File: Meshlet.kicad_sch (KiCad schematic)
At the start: 93 parts, among them J1 Ext. Notif. Header, J10 STEMMA QT I2C, J11 GPIO Exp., J12 I2C PINHEADER, J2 USB_C_Receptacle_USB2.0_16P, J3 Ext. Power Header, J4 Batt. Header (JST-PH 2.0), J5 SWD, J6 Batt. Header (Picoblade 1.25), J7 GPS Header, J8 User Btn Header, J9 Power Switch, Q1 AO3400A, SW1 BOOTSEL, SW3 RST, U1 W25Q32JVZP, U2 XC6206PxxxMR, U3 RP2350_60QFN, U4 INA3221, U5 BME280, U6 Wio-SX1262, U7 USBLC6-2SC6, U8 BQ24074RGT, Y1 12.000MHz

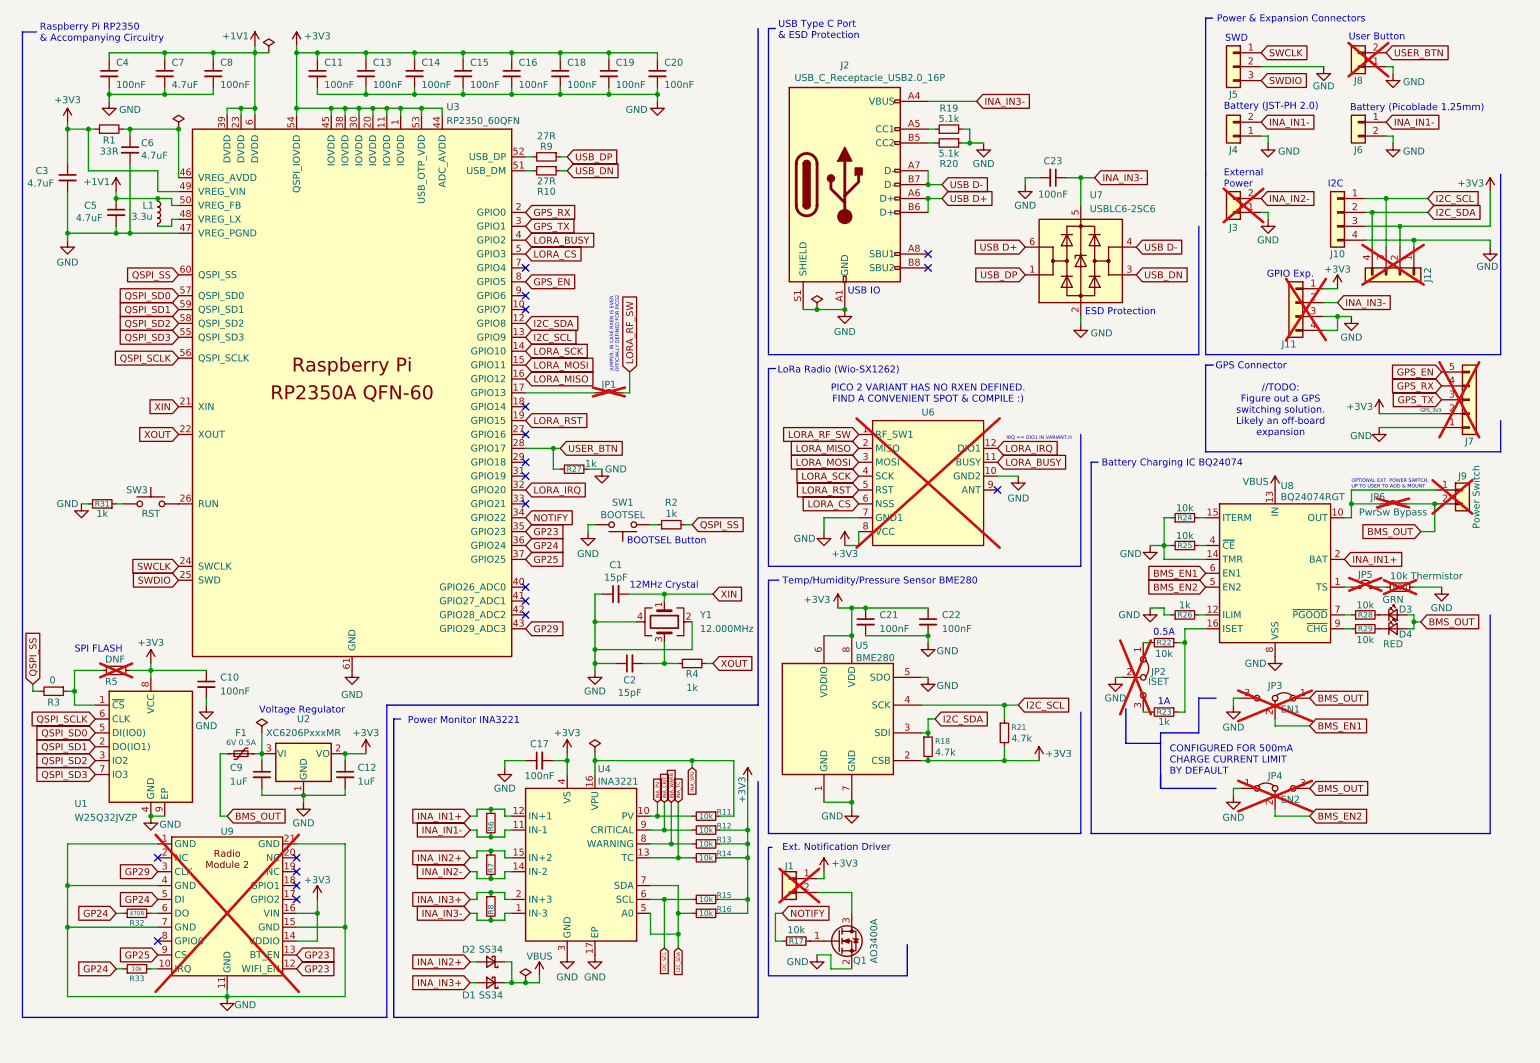
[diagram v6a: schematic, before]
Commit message: Silkscreen changes, added BQ24074 output breakout
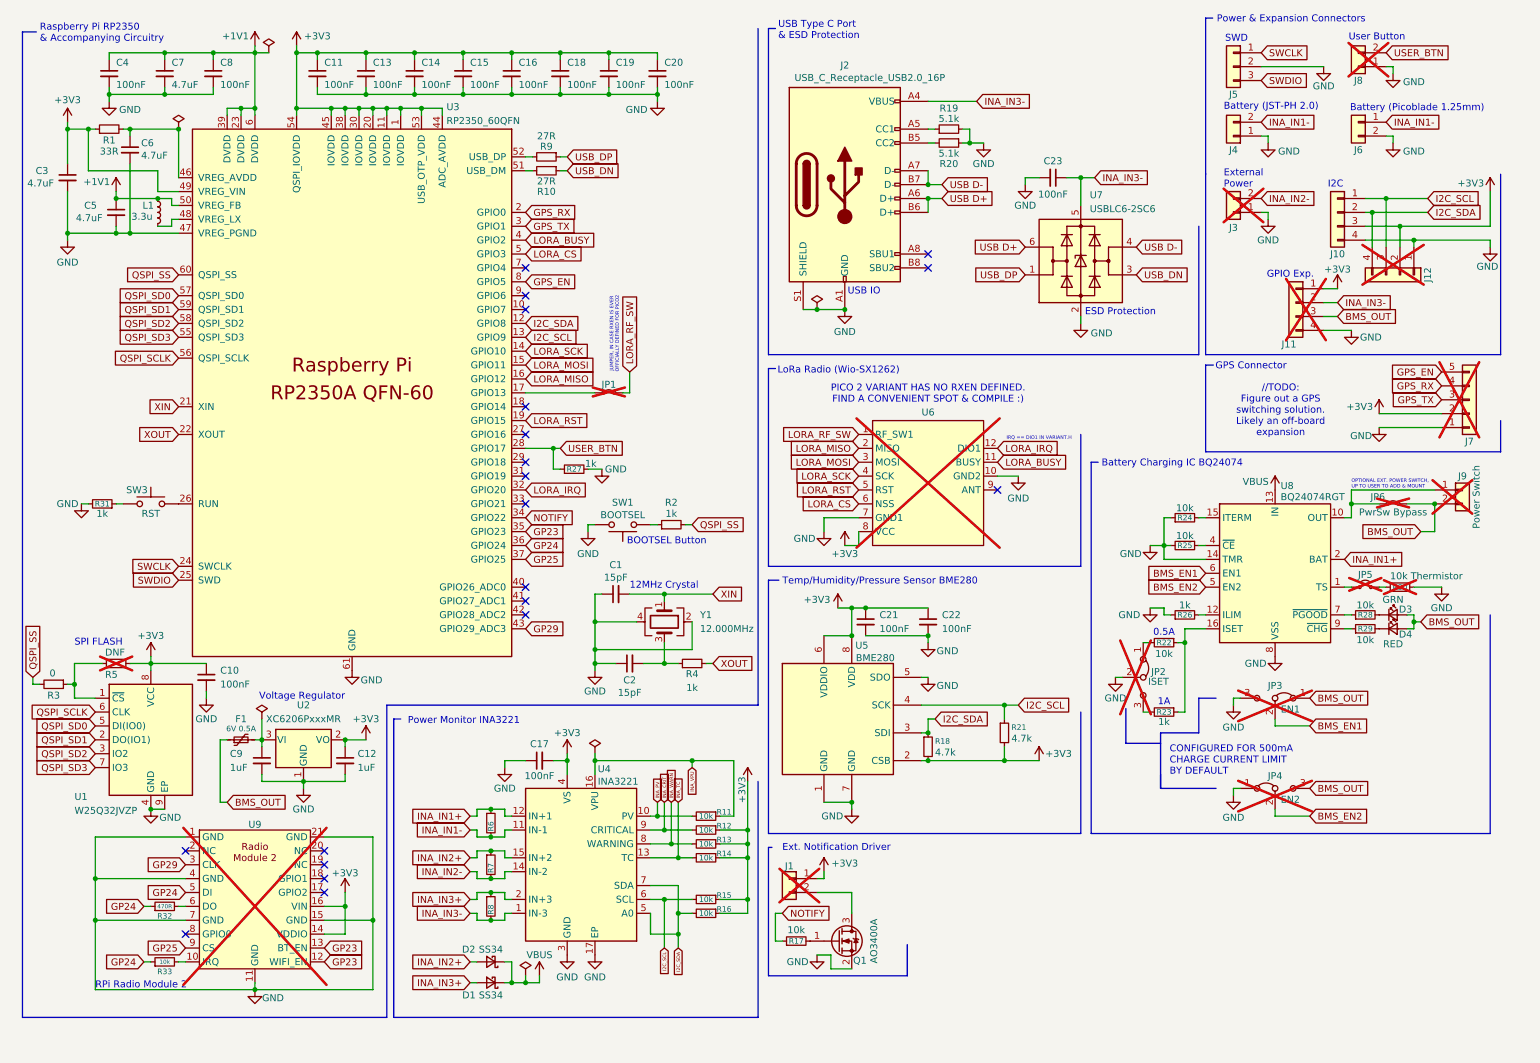
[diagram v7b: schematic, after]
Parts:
- R6, R7, R8: value PT2512FK-070R1L -> PA2512FKF7W0R01E
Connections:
- net BMS_OUT: now also J11.3 (Pin_3)
- net GND: no longer J11.3 (Pin_3)
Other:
- note added: "RPi Radio Module 2"
- moved on the sheet: C10, C12, C9, F1, R3, R32, R33, R5, U1, U2, U9

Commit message: Fixed several design flaws. More caps, more LDOs, etc
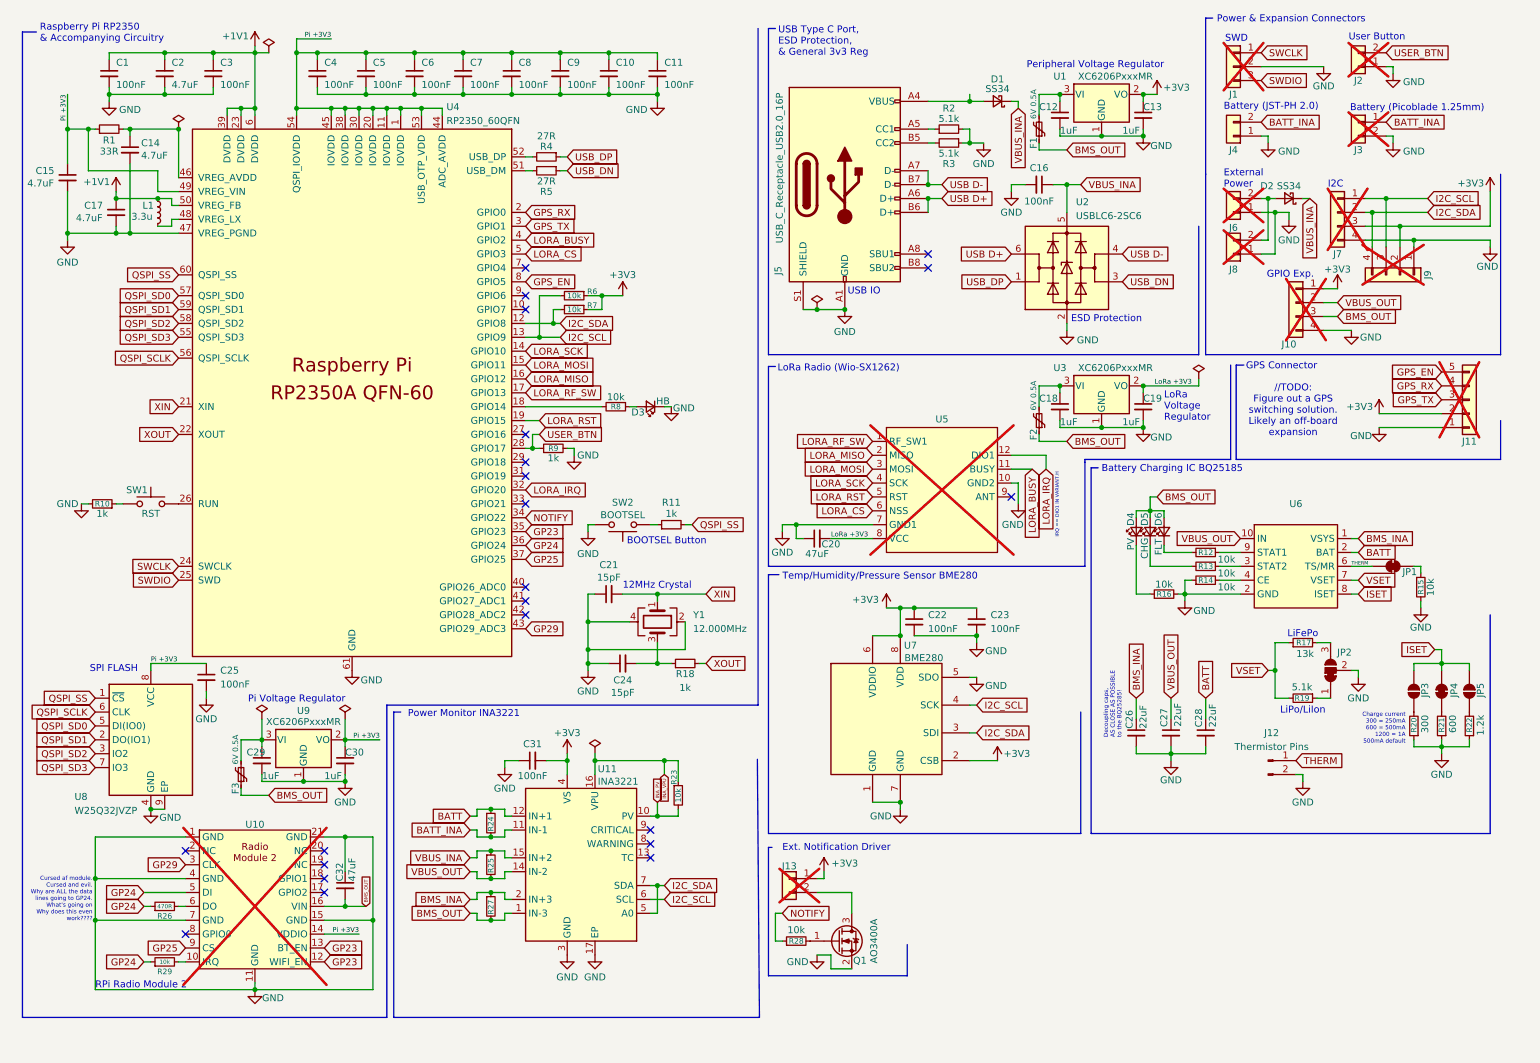
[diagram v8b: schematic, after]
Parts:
- removed J9: Power Switch, Connector_PinHeader_2.00mm:PinHeader_1x02_P2.00mm_Vertical, symbol Connector_Generic:Conn_01x02
- removed JP1: RF_SW Jumper, Jumper:SolderJumper-2_P1.3mm_Bridged_RoundedPad1.0x1.5mm, symbol Jumper:Jumper_2_Small_Bridged
- removed JP2: ISET, Jumper:SolderJumper-3_P1.3mm_Bridged12_RoundedPad1.0x1.5mm, symbol Jumper:Jumper_3_Bridged12
- removed JP3: EN1, Jumper:SolderJumper-3_P1.3mm_Bridged12_RoundedPad1.0x1.5mm, symbol Jumper:Jumper_3_Bridged12
- removed JP4: EN2, Jumper:SolderJumper-3_P1.3mm_Bridged12_RoundedPad1.0x1.5mm, symbol Jumper:Jumper_3_Bridged12
- removed JP5: BMS TS Jumper, Jumper:SolderJumper-2_P1.3mm_Open_RoundedPad1.0x1.5mm, symbol Jumper:Jumper_2_Small_Open
- removed JP6: PwrSw Bypass, Jumper:SolderJumper-2_P1.3mm_Bridged_RoundedPad1.0x1.5mm, symbol Jumper:Jumper_2_Small_Bridged
- removed R12, R13, R14, R24: 10k, Resistor_SMD:R_0402_1005Metric, symbol Device:R_Small
- removed R18: 4.7k, Resistor_SMD:R_0402_1005Metric, symbol Device:R_Small
- removed R23, R26: 1k, Resistor_SMD:R_0402_1005Metric, symbol Device:R_Small
- removed R3: 0, Resistor_SMD:R_0402_1005Metric, symbol Device:R_Small
- removed R30: 10k Thermistor, Resistor_SMD:R_0402_1005Metric, symbol Device:R_Small
- removed R5: DNF, Resistor_SMD:R_0402_1005Metric, symbol Device:R_Small
- removed U8: BQ24074RGT, Package_DFN_QFN:VQFN-16-1EP_3x3mm_P0.5mm_EP1.6x1.6mm, symbol Battery_Management:BQ24074RGT
- added C12, C13, C18, C19: 1uF, Capacitor_SMD:C_0402_1005Metric, symbol Device:C_Small
- added C20, C32: 47uF, Capacitor_SMD:C_0805_2012Metric, symbol Device:C_Small
- added C26, C27, C28: 22uF, symbol Device:C_Small
- added D3: HB, LED_SMD:LED_0603_1608Metric, symbol Device:LED_Small
- added D4: PV, LED_SMD:LED_0603_1608Metric, symbol Device:LED_Small
- added F1, F2: 6V 0.5A, Fuse:Fuse_0603_1608Metric, symbol Device:Polyfuse_Small
- added J12: Thermistor Pins, symbol Connector:Conn_01x02_Pin
- added J8: Ext. Power Header, Connector_PinHeader_2.54mm:PinHeader_1x02_P2.54mm_Vertical, symbol Connector_Generic:Conn_01x02
- added JP1: TS, symbol Jumper:SolderJumper_2_Bridged
- added JP2: Chemistry Select, symbol Jumper:SolderJumper_3_Bridged12
- added JP3, JP5: SolderJumper_2_Open, symbol Jumper:SolderJumper_2_Open
- added JP4: SolderJumper_2_Bridged, symbol Jumper:SolderJumper_2_Bridged
- added R15, R16, R8: 10k, Resistor_SMD:R_0402_1005Metric, symbol Device:R_Small
- added R17: 13k, symbol Device:R_Small
- added R19: 5.1k, symbol Device:R_Small
- added R20: 300, symbol Device:R_Small
- added U1, U3: XC6206PxxxMR, Package_TO_SOT_SMD:SOT-23-3, symbol Regulator_Linear:XC6206PxxxMR
- added U6: ~, symbol BQ25185:BQ25185
- D5: renamed from D3; value GRN -> CHG
- D6: renamed from D4; value RED -> FLT
- J1: renamed from J5; now not fitted
- J3: renamed from J6; now not fitted
- J7: renamed from J10; now not fitted
- R21: value 4.7k -> 600; footprint Resistor_SMD:R_0402_1005Metric -> (none); LCSC C25900 -> (none)
- R22: value 10k -> 1.2k; footprint Resistor_SMD:R_0402_1005Metric -> (none); LCSC C25744 -> (none)
- renumbered C4 to C1, C19 to C10, C20 to C11, C6 to C14, C3 to C15, C23 to C16, C5 to C17, C7 to C2, C1 to C21, C21 to C22, C22 to C23, C2 to C24, C10 to C25, C9 to C29, C8 to C3, C12 to C30, C17 to C31, C11 to C4, C13 to C5, C14 to C6, C15 to C7, C16 to C8, C18 to C9, D2 to D1, D1 to D2, F1 to F3, J11 to J10, J7 to J11, J1 to J13, J8 to J2, J2 to J5, J3 to J6, J12 to J9, R31 to R10, R2 to R11, R29 to R12, R28 to R13, R25 to R14, R4 to R18, R19 to R2, R11 to R23, R6 to R24, R7 to R25, R32 to R26, R8 to R27, R17 to R28, R33 to R29, R20 to R3, R9 to R4, R10 to R5, R15 to R6, R16 to R7, R27 to R9, SW3 to SW1, SW1 to SW2, U9 to U10, U4 to U11, U7 to U2, U3 to U4, U6 to U5, U5 to U7, U1 to U8, U2 to U9
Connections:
- net VBUS is gone; now on net VBUS_INA: D1.1 (K), D2.1 (K)
- net +3V3: now also C13.1, U1.2 (VO); no longer C10.1, C11.1, C15.1, C25.1, C30.1, C4.1, C5.1, C6.1, C7.1, C8.1, C9.1, R1.1, R21.2, U10.14 (VDDIO), U10.16 (VIN), U4.1 (IOVDD), U4.11 (IOVDD), U4.20 (IOVDD), U4.30 (IOVDD), U4.38 (IOVDD), U4.44 (ADC_AVDD), U4.45 (IOVDD), U4.49 (VREG_VIN), U4.53 (USB_OTP_VDD), U4.54 (QSPI_IOVDD), U5.8 (VCC), U8.8 (VCC), U9.2 (VO)
- net BMS_OUT: now also R27.2, U10.16 (VIN), U11.1 (IN-3), C32.2, D4.2 (A), F1.1, F2.1
- net GND: now also R14.1, R21.1, R22.1, C12.2, C13.2, C18.2, C19.2, C20.1, C26.2, C27.2, C28.2, C32.1, D3.1 (K), J12.2 (Pin_2), J8.1 (Pin_1), JP2.2 (C), R15.2, R16.2, R20.1, U1.1 (GND), U3.1 (GND), U6.2 (BAT); no longer R14.2
- net I2C_SCL: no longer R21.1
- net LORA_RF_SW: now also U4.17 (GPIO13)
- net QSPI_SS: now also U8.1 (~{CS})
- net at R22.2: now also JP5.1 (A)
- net at R12.1: now also U6.9 (STAT1)
- net at R13.1: now also U6.3 (STAT2)
- net at U4.18 (GPIO14): now also R8.2
- net INA_CRIT: no longer names the net of U11.9 (CRITICAL)
- net INA_IN1+ renamed BATT
- net BATT: now also C28.1, U6.2 (BAT)
- net INA_IN1- renamed BATT_INA
- net INA_IN2+ renamed VBUS_INA
- net VBUS_INA: now also C16.1, U2.5 (VBUS); no longer D1.2 (A)
- net INA_IN2- renamed VBUS_OUT
- net VBUS_OUT: now also J10.2 (Pin_2), C27.1, U6.10 (IN); no longer J6.2 (Pin_2)
- net INA_IN3+ renamed BMS_INA
- net BMS_INA: now also C26.1, U6.1 (VSYS); no longer D2.2 (A)
- removed net INA_IN3-: C16.1, J10.2 (Pin_2), J5.A4 (VBUS), J5.A9 (VBUS), J5.B4 (VBUS), J5.B9 (VBUS), R27.2, U11.1 (IN-3), U2.5 (VBUS)
- net INA_TC: no longer names the net of U11.13 (TC)
- net INA_WARN: no longer names the net of U11.8 (WARNING)
- new net: D3.2 (A), R8.1
- new net: C18.1, F2.2, U3.3 (VI)
- new net: D4.1 (K), R16.1
- new net: JP2.3 (B), R17.2
- new net: JP4.1 (A), R21.2
- new net: C12.1, F1.2, U1.3 (VI)
- new net: JP2.1 (A), R19.1
- new net: D1.2 (A), J5.A4 (VBUS), J5.A9 (VBUS), J5.B4 (VBUS), J5.B9 (VBUS)
- new net: D2.2 (A), J6.2 (Pin_2), J8.2 (Pin_2)
- new net: JP3.1 (A), R20.2
- new net: R14.2, U6.4 (CE)
- new net: JP1.2 (B), R15.1
- new net ISET: JP3.2 (B), JP4.2 (B), JP5.2 (B), U6.8 (ISET)
- new net LoRa +3V3: C19.1, C20.2, U3.2 (VO), U5.8 (VCC)
- new net Pi +3V3: C10.1, C11.1, C15.1, C25.1, C30.1, C4.1, C5.1, C6.1, C7.1, C8.1, C9.1, R1.1, U10.14 (VDDIO), U4.1 (IOVDD), U4.11 (IOVDD), U4.20 (IOVDD), U4.30 (IOVDD), U4.38 (IOVDD), U4.44 (ADC_AVDD), U4.45 (IOVDD), U4.49 (VREG_VIN), U4.53 (USB_OTP_VDD), U4.54 (QSPI_IOVDD), U8.8 (VCC), U9.2 (VO)
- new net THERM: J12.1 (Pin_1), JP1.1 (A), U6.6 (TS/MR)
- new net VSET: R17.1, R19.2, U6.7 (VSET)
- no-connect marks 20 -> 22
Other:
- note added: "Battery Charging IC BQ25185"
- note added: "Charge current 300 = 250mA 600 = 500mA 1200 = 1A 500mA default"
- note added: "Cursed af module. Cursed and evil. Why are ALL the data lines going to GP24. What's going on Why does this even work????"
- note added: "Decoupling caps, AS CLOSE AS POSSIBLE to the BQ25285!"
- note added: "LiFePo"
- note added: "LiPo/LiIon"
- note added: "LoRa Voltage Regulator"
- note added: "Peripheral Voltage Regulator"
- note added: "Pi Voltage Regulator"
- note added: "USB Type C Port, ESD Protection, & General 3v3 Reg"
- note removed: "0.5A"
- note removed: "1A"
- note removed: "Battery Charging IC BQ24074"
- note removed: "CONFIGURED FOR 500mA CHARGE CURRENT LIMIT BY DEFAULT"
- note removed: "JUMPER, IN CASE RXEN IS EVER OFFICIALLY DEFINED FOR PICO2"
- note removed: "OPTIONAL EXT. POWER SWITCH, UP TO USER TO ADD & MOUNT"
- note removed: "PICO 2 VARIANT HAS NO RXEN DEFINED. FIND A CONVENIENT SPOT & COMPILE :)"
- note removed: "USB Type C Port & ESD Protection"
- note removed: "Voltage Regulator"
- moved on the sheet: C16, C21, C22, C23, C24, C31, D1, D2, D5, D6, F3, R12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
